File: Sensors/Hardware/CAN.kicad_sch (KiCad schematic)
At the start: 12 parts, among them U20 SN65HVD230

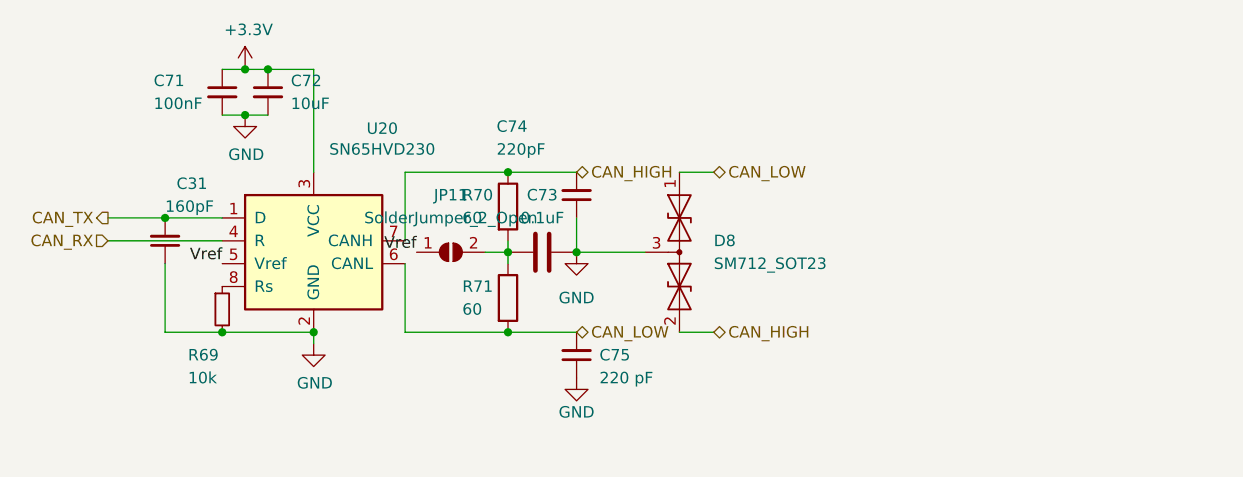
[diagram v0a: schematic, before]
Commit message: integrated new ESP32-s3
Need to remove excess thermocouples
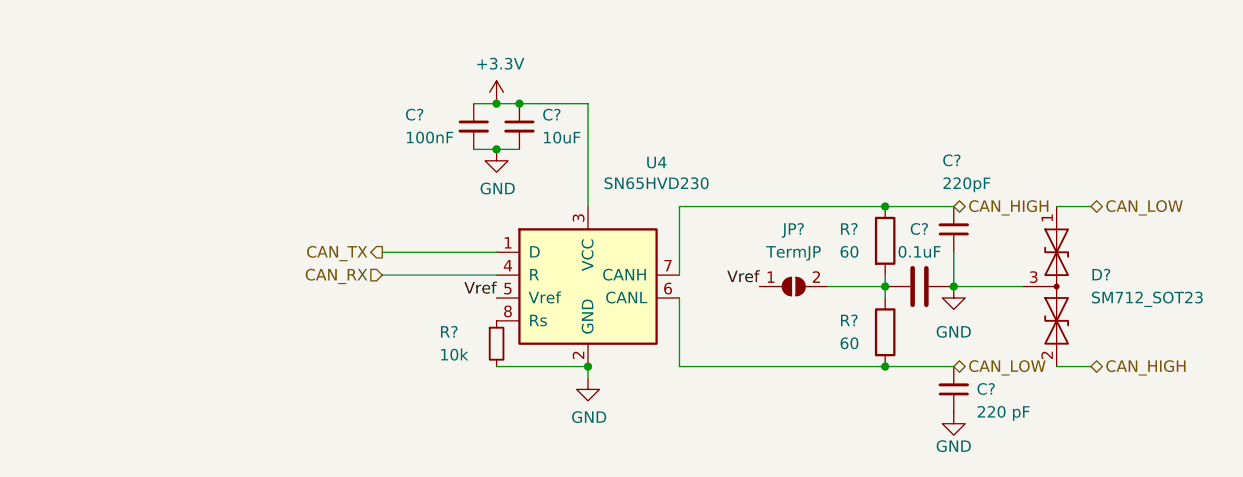
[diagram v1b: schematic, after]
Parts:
- removed C31: 160pF, Capacitor_SMD:C_0603_1608Metric, symbol Device:C_Small
- removed C71: 100nF, Capacitor_SMD:C_0603_1608Metric, symbol Device:C_Small
- removed C72: 10uF, Capacitor_SMD:C_0603_1608Metric, symbol Device:C_Small
- removed C73: 0.1uF, Capacitor_SMD:C_0603_1608Metric, symbol Device:C
- removed C74: 220pF, Capacitor_SMD:C_0603_1608Metric, symbol Device:C_Small
- removed C75: 220 pF, Capacitor_SMD:C_0603_1608Metric, symbol Device:C_Small
- removed D8: SM712_SOT23, Package_TO_SOT_SMD:SOT-23, symbol Diode:SM712_SOT23
- removed JP11: SolderJumper_2_Open, Jumper:SolderJumper-2_P1.3mm_Open_RoundedPad1.0x1.5mm, symbol Jumper:SolderJumper_2_Open
- removed R69: 10k, Resistor_SMD:R_0603_1608Metric, symbol Device:R_Small
- removed R70, R71: 60, Resistor_SMD:R_0603_1608Metric, symbol Device:R
- removed U20: SN65HVD230, Package_SO:SOIC-8_3.9x4.9mm_P1.27mm, symbol Interface_CAN_LIN:SN65HVD230
- added C?: 10uF, Capacitor_SMD:C_0603_1608Metric, symbol Device:C_Small
- added C?: 220pF, Capacitor_SMD:C_0402_1005Metric, symbol Device:C_Small
- added C?: 100nF, Capacitor_SMD:C_0402_1005Metric, symbol Device:C_Small
- added C?: 0.1uF, Capacitor_SMD:C_0402_1005Metric, symbol Device:C
- added C?: 220 pF, Capacitor_SMD:C_0402_1005Metric, symbol Device:C_Small
- added D?: SM712_SOT23, Package_TO_SOT_SMD:SOT-23, symbol Diode:SM712_SOT23
- added JP?: TermJP, symbol Jumper:SolderJumper_2_Open
- added R?: 10k, Resistor_SMD:R_0402_1005Metric, symbol Device:R_Small
- added R? (x2): 60, Resistor_SMD:R_0402_1005Metric, symbol Device:R
- added U4: SN65HVD230, Package_SO:SOIC-8_3.9x4.9mm_P1.27mm, symbol Interface_CAN_LIN:SN65HVD230
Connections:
- net +3V3: now also C?.1, C?.1, U4.3 (VCC)
- net CAN_HIGH: now also C?.2, D?.2 (A2), R?.1, U4.7 (CANH)
- net CAN_LOW: now also C?.2, D?.1 (A1), R?.2, U4.6 (CANL)
- net CAN_RX: now also U4.4 (R)
- net CAN_TX: now also U4.1 (D)
- net GND: now also C?.1, C?.1, C?.2, C?.2, C?.2, D?.3 (common), R?.2, U4.2 (GND)
- net Vref: now also JP?.1 (A), U4.5 (Vref)
- new net: R?.1, U4.8 (Rs)
- new net: C?.1, JP?.2 (B), R?.1, R?.2

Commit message: added template changes
Moved power to seperate file
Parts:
- R?: value 10k -> 0
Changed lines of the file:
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@@
       (effects (font (size 1.27 1.27)) (justify left))
     )
-    (property "Value" "10k" (id 1) (at 118.11 96.52 0)
+    (property "Value" "0" (id 1) (at 118.11 96.52 0)
       (effects (font (size 1.27 1.27)) (justify left))
     )

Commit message: fp assignments
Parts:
- C59: renamed from C?; footprint Capacitor_SMD:C_0603_1608Metric -> Capacitor_SMD:C_0402_1005Metric
- JP37: renamed from JP?; footprint (none) -> Jumper:SolderJumper-2_P1.3mm_Open_RoundedPad1.0x1.5mm
- gave numbers to parts that had none: 8
- renumbered U4 to U13
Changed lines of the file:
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@@
   (symbol (lib_id "power:GND") (at 134.62 99.06 0) (unit 1)
     (in_bom yes) (on_board yes) (fields_autoplaced)
-    (property "Reference" "#PWR?" (id 0) (at 134.62 105.41 0)
+    (property "Reference" "#PWR0154" (id 0) (at 134.62 105.41 0)
       (effects (font (size 1.27 1.27)) hide)
     )
@@
   (symbol (lib_id "power:+3.3V") (at 124.46 68.58 0) (unit 1)
     (in_bom yes) (on_board yes) (fields_autoplaced)
-    (property "Reference" "#PWR?" (id 0) (at 124.46 72.39 0)
+    (property "Reference" "#PWR0152" (id 0) (at 124.46 72.39 0)
       (effects (font (size 1.27 1.27)) hide)
     )
@@
   (symbol (lib_id "Interface_CAN_LIN:SN65HVD230") (at 134.62 87.63 0) (unit 1)
     (in_bom yes) (on_board yes) (fields_autoplaced)
-    (property "Reference" "U?" (id 0) (at 142.24 75.1586 0))
+    (property "Reference" "U13" (id 0) (at 142.24 75.1586 0))
     (property "Value" "SN65HVD230" (id 1) (at 142.24 77.47 0))
     (property "Footprint" "Package_SO:SOIC-8_3.9x4.9mm_P1.27mm" (id 2) (at 134.62 100.33 0)
@@
   (symbol (lib_id "Device:C_Small") (at 127 71.12 0) (unit 1)
     (in_bom yes) (on_board yes) (fields_autoplaced)
-    (property "Reference" "C?" (id 0) (at 129.54 69.8562 0)
+    (property "Reference" "C59" (id 0) (at 129.54 69.8562 0)
       (effects (font (size 1.27 1.27)) (justify left))
     )
@@
       (effects (font (size 1.27 1.27)) (justify left))
     )
-    (property "Footprint" "Capacitor_SMD:C_0603_1608Metric" (id 2) (at 127 71.12 0)
+    (property "Footprint" "Capacitor_SMD:C_0402_1005Metric" (id 2) (at 127 71.12 0)
       (effects (font (size 1.27 1.27)) hide)
     )
@@
   (symbol (lib_id "Device:C_Small") (at 175.26 82.55 180) (unit 1)
     (in_bom yes) (on_board yes)
-    (property "Reference" "C?" (id 0) (at 173.99 74.93 0)
+    (property "Reference" "C61" (id 0) (at 173.99 74.93 0)
       (effects (font (size 1.27 1.27)) (justify right))
     )
@@
   (symbol (lib_id "Diode:SM712_SOT23") (at 186.69 88.9 270) (unit 1)
     (in_bom yes) (on_board yes) (fields_autoplaced)
-    (property "Reference" "D?" (id 0) (at 190.5 87.63 90)
+    (property "Reference" "D3" (id 0) (at 190.5 87.63 90)
       (effects (font (size 1.27 1.27)) (justify left))
     )
@@
   (symbol (lib_id "power:GND") (at 175.26 88.9 0) (unit 1)
     (in_bom yes) (on_board yes) (fields_autoplaced)
-    (property "Reference" "#PWR?" (id 0) (at 175.26 95.25 0)
+    (property "Reference" "#PWR0155" (id 0) (at 175.26 95.25 0)
       (effects (font (size 1.27 1.27)) hide)
     )
@@
   (symbol (lib_id "power:GND") (at 175.26 102.87 0) (unit 1)
     (in_bom yes) (on_board yes) (fields_autoplaced)
-    (property "Reference" "#PWR?" (id 0) (at 175.26 109.22 0)
+    (property "Reference" "#PWR0156" (id 0) (at 175.26 109.22 0)
       (effects (font (size 1.27 1.27)) hide)
     )
@@
   (symbol (lib_id "Device:C_Small") (at 121.92 71.12 0) (unit 1)
     (in_bom yes) (on_board yes) (fields_autoplaced)
-    (property "Reference" "C?" (id 0) (at 114.3 69.85 0)
+    (property "Reference" "C58" (id 0) (at 114.3 69.85 0)
       (effects (font (size 1.27 1.27)) (justify left))
     )
@@
   (symbol (lib_id "Device:R_Small") (at 124.46 95.25 0) (unit 1)
     (in_bom yes) (on_board yes)
-    (property "Reference" "R?" (id 0) (at 118.11 93.98 0)
+    (property "Reference" "R69" (id 0) (at 118.11 93.98 0)
       (effects (font (size 1.27 1.27)) (justify left))
     )
@@
   (symbol (lib_id "Device:R") (at 167.64 93.98 0) (unit 1)
     (in_bom yes) (on_board yes) (fields_autoplaced)
-    (property "Reference" "R?" (id 0) (at 162.56 92.71 0)
+    (property "Reference" "R71" (id 0) (at 162.56 92.71 0)
       (effects (font (size 1.27 1.27)) (justify left))
     )
@@
   (symbol (lib_id "Device:R") (at 167.64 83.82 0) (unit 1)
     (in_bom yes) (on_board yes) (fields_autoplaced)
-    (property "Reference" "R?" (id 0) (at 162.56 82.55 0)
+    (property "Reference" "R70" (id 0) (at 162.56 82.55 0)
       (effects (font (size 1.27 1.27)) (justify left))
     )
@@
   (symbol (lib_id "Device:C") (at 171.45 88.9 90) (unit 1)
     (in_bom yes) (on_board yes) (fields_autoplaced)
-    (property "Reference" "C?" (id 0) (at 171.45 82.55 90))
+    (property "Reference" "C60" (id 0) (at 171.45 82.55 90))
     (property "Value" "0.1uF" (id 1) (at 171.45 85.09 90))
     (property "Footprint" "Capacitor_SMD:C_0402_1005Metric" (id 2) (at 175.26 87.9348 0)
@@
   (symbol (lib_id "power:GND") (at 124.46 73.66 0) (unit 1)
     (in_bom yes) (on_board yes) (fields_autoplaced)
-    (property "Reference" "#PWR?" (id 0) (at 124.46 80.01 0)
+    (property "Reference" "#PWR0153" (id 0) (at 124.46 80.01 0)
       (effects (font (size 1.27 1.27)) hide)
     )
@@
   (symbol (lib_id "Jumper:SolderJumper_2_Open") (at 157.48 88.9 0) (unit 1)
     (in_bom yes) (on_board yes) (fields_autoplaced)
-    (property "Reference" "JP?" (id 0) (at 157.48 82.55 0))
+    (property "Reference" "JP37" (id 0) (at 157.48 82.55 0))
     (property "Value" "TermJP" (id 1) (at 157.48 85.09 0))
-    (property "Footprint" "" (id 2) (at 157.48 88.9 0)
+    (property "Footprint" "Jumper:SolderJumper-2_P1.3mm_Open_RoundedPad1.0x1.5mm" (id 2) (at 157.48 88.9 0)
       (effects (font (size 1.27 1.27)) hide)
     )
@@
   (symbol (lib_id "Device:C_Small") (at 175.26 100.33 180) (unit 1)
     (in_bom yes) (on_board yes) (fields_autoplaced)
-    (property "Reference" "C?" (id 0) (at 177.8 100.33 0)
+    (property "Reference" "C62" (id 0) (at 177.8 100.33 0)
       (effects (font (size 1.27 1.27)) (justify right))
     )

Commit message: update (tps and filters)
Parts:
- R69, R70, R71: footprint Resistor_SMD:R_0402_1005Metric -> Resistor_SMD:R_0603_1608Metric
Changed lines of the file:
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@@
       (effects (font (size 1.27 1.27)) (justify left))
     )
-    (property "Footprint" "Resistor_SMD:R_0402_1005Metric" (id 2) (at 124.46 95.25 0)
+    (property "Footprint" "Resistor_SMD:R_0603_1608Metric" (id 2) (at 124.46 95.25 0)
       (effects (font (size 1.27 1.27)) hide)
     )
@@
       (effects (font (size 1.27 1.27)) (justify left))
     )
-    (property "Footprint" "Resistor_SMD:R_0402_1005Metric" (id 2) (at 165.862 93.98 90)
+    (property "Footprint" "Resistor_SMD:R_0603_1608Metric" (id 2) (at 165.862 93.98 90)
       (effects (font (size 1.27 1.27)) hide)
     )
@@
       (effects (font (size 1.27 1.27)) (justify left))
     )
-    (property "Footprint" "Resistor_SMD:R_0402_1005Metric" (id 2) (at 165.862 83.82 90)
+    (property "Footprint" "Resistor_SMD:R_0603_1608Metric" (id 2) (at 165.862 83.82 90)
       (effects (font (size 1.27 1.27)) hide)
     )

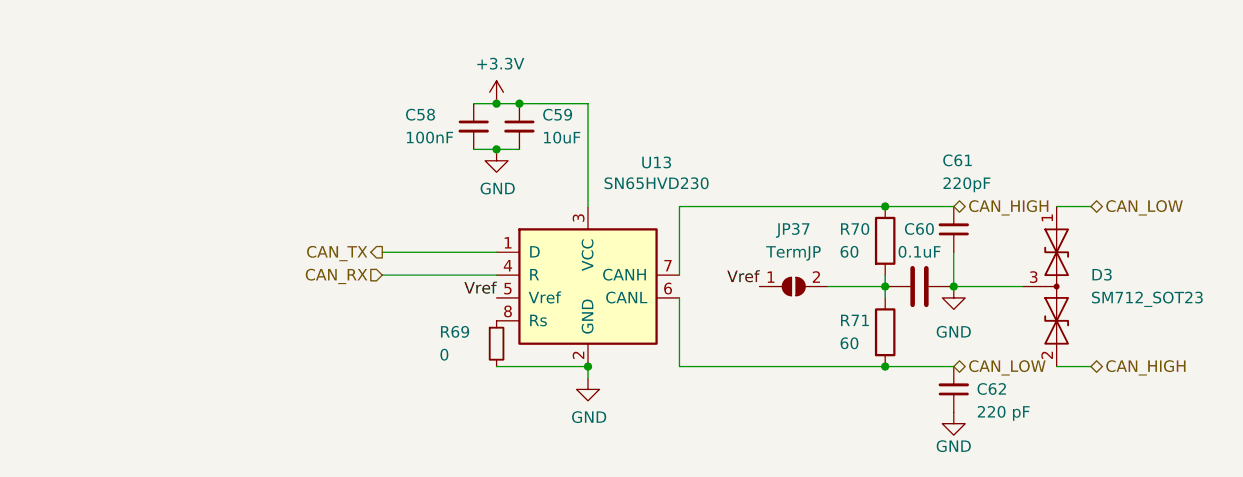
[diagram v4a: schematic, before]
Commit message: ADC connections and KiCAD version update
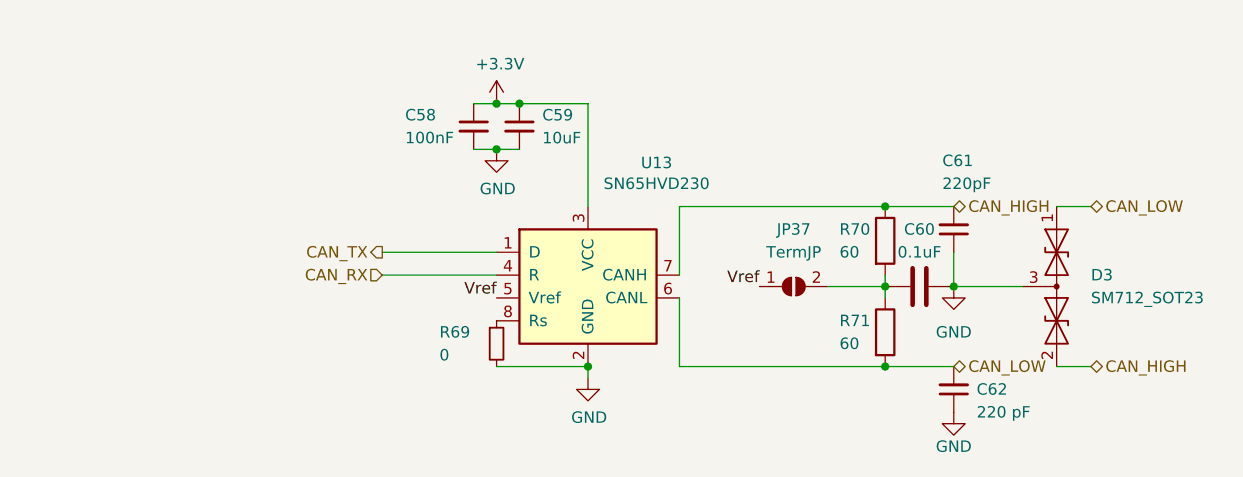
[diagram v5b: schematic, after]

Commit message: added LEDS and CAN connections
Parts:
- C58, C59, C60, C61, C62: footprint Capacitor_SMD:C_0402_1005Metric -> Capacitor_SMD:C_0603_1608Metric
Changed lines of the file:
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@@
       (effects (font (size 1.27 1.27)) (justify left))
     )
-    (property "Footprint" "Capacitor_SMD:C_0402_1005Metric" (at 127 71.12 0)
+    (property "Footprint" "Capacitor_SMD:C_0603_1608Metric" (at 127 71.12 0)
       (effects (font (size 1.27 1.27)) hide)
     )
@@
       (effects (font (size 1.27 1.27)) (justify right))
     )
-    (property "Footprint" "Capacitor_SMD:C_0402_1005Metric" (at 175.26 82.55 0)
+    (property "Footprint" "Capacitor_SMD:C_0603_1608Metric" (at 175.26 82.55 0)
       (effects (font (size 1.27 1.27)) hide)
     )
@@
       (effects (font (size 1.27 1.27)) (justify left))
     )
-    (property "Footprint" "Capacitor_SMD:C_0402_1005Metric" (at 121.92 71.12 0)
+    (property "Footprint" "Capacitor_SMD:C_0603_1608Metric" (at 121.92 71.12 0)
       (effects (font (size 1.27 1.27)) hide)
     )
@@
       (effects (font (size 1.27 1.27)))
     )
-    (property "Footprint" "Capacitor_SMD:C_0402_1005Metric" (at 175.26 87.9348 0)
+    (property "Footprint" "Capacitor_SMD:C_0603_1608Metric" (at 175.26 87.9348 0)
       (effects (font (size 1.27 1.27)) hide)
     )
@@
       (effects (font (size 1.27 1.27)) (justify right))
     )
-    (property "Footprint" "Capacitor_SMD:C_0402_1005Metric" (at 175.26 100.33 0)
-      (effects (font (size 1.27 1.27)) hide)
-    )
+    (property "Footprint" "Capacitor_SMD:C_0603_1608Metric" (at 175.26 100.33 0)
+      (effects (font (size 1.27 1.27)) hide)
+    )

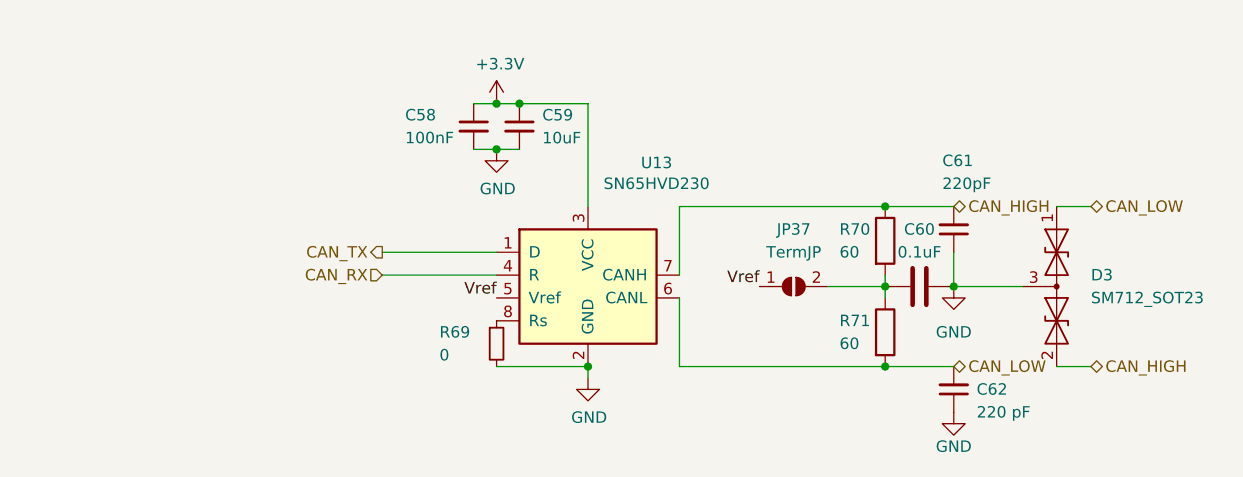
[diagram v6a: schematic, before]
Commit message: Schematic update
unfinished
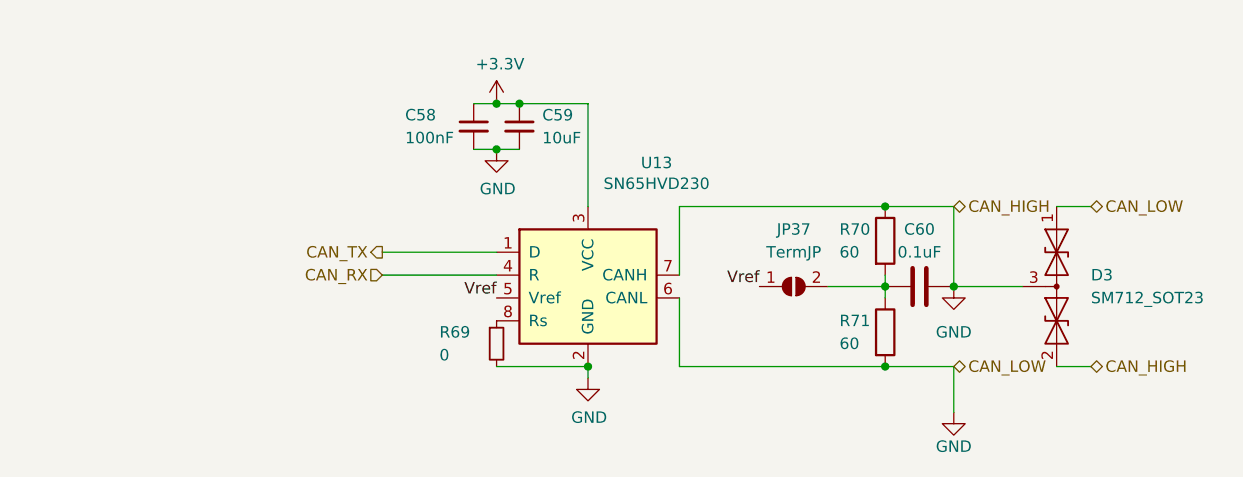
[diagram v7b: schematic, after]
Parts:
- removed C61: 220pF, Capacitor_SMD:C_0603_1608Metric, symbol Device:C_Small
- removed C62: 220 pF, Capacitor_SMD:C_0603_1608Metric, symbol Device:C_Small
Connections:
- net CAN_HIGH is gone; now on net GND: D3.2 (A2), R70.1, U13.7 (CANH)
- net CAN_LOW is gone; now on net GND: D3.1 (A1), R71.2, U13.6 (CANL)
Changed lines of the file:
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@@
     (stroke (width 0) (type default))
   )
-  (wire (pts (xy 175.26 85.09) (xy 175.26 88.9))
+  (wire (pts (xy 175.26 80.01) (xy 175.26 88.9))
     (stroke (width 0) (type default))
   )
@@
   )
   (wire (pts (xy 111.76 87.63) (xy 124.46 87.63))
+    (stroke (width 0) (type default))
+  )
+  (wire (pts (xy 175.26 97.79) (xy 175.26 102.87))
     (stroke (width 0) (type default))
   )
@@
     )
   )
-  (symbol (lib_id "Device:C_Small") (at 175.26 82.55 180) (unit 1)
-    (in_bom yes) (on_board yes) (dnp no)
-    (property "Reference" "C61" (at 173.99 74.93 0)
-      (effects (font (size 1.27 1.27)) (justify right))
-    )
-    (property "Value" "220pF" (at 173.99 77.47 0)
-      (effects (font (size 1.27 1.27)) (justify right))
-    )
-    (property "Footprint" "Capacitor_SMD:C_0603_1608Metric" (at 175.26 82.55 0)
-      (effects (font (size 1.27 1.27)) hide)
-    )
-    (property "Datasheet" "~" (at 175.26 82.55 0)
-      (effects (font (size 1.27 1.27)) hide)
-    )
-    (pin "1")
-    (pin "2")
-    (instances
-      (project "sensorboard"
-        (path "/26801cfb-b53b-4a6a-a2f4-5f4986565765/f5d08e6e-78a9-4643-8dbf-1f1240e72106"
-          (reference "C61") (unit 1)
-        )
-      )
-    )
-  )
   (symbol (lib_id "Diode:SM712_SOT23") (at 186.69 88.9 270) (unit 1)
     (in_bom yes) (on_board yes) (dnp no) (fields_autoplaced)
@@
         )
       )
-    )
-  )
-  (symbol (lib_id "Device:C_Small") (at 175.26 100.33 180) (unit 1)
-    (in_bom yes) (on_board yes) (dnp no) (fields_autoplaced)
-    (property "Reference" "C62" (at 177.8 100.33 0)
-      (effects (font (size 1.27 1.27)) (justify right))
-    )
-    (property "Value" "220 pF" (at 177.8 102.87 0)
-      (effects (font (size 1.27 1.27)) (justify right))
-    )
-    (property "Footprint" "Capacitor_SMD:C_0603_1608Metric" (at 175.26 100.33 0)
-      (effects (font (size 1.27 1.27)) hide)
-    )
-    (property "Datasheet" "~" (at 175.26 100.33 0)
-      (effects (font (size 1.27 1.27)) hide)
-    )
-    (pin "1")
-    (pin "2")
-    (instances
-      (project "sensorboard"
-        (path "/26801cfb-b53b-4a6a-a2f4-5f4986565765/f5d08e6e-78a9-4643-8dbf-1f1240e72106"
-          (reference "C62") (unit 1)
-        )
-      )
